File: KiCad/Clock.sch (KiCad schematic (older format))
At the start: 20 parts, among them SW2 SW_Push, SW3 SW_Push_SPDT, U44 NE555DR, U45 SN74LVC1G125DCK, U47 SN74LVC1G32DCK, U48 SN74LVC1G125DCK

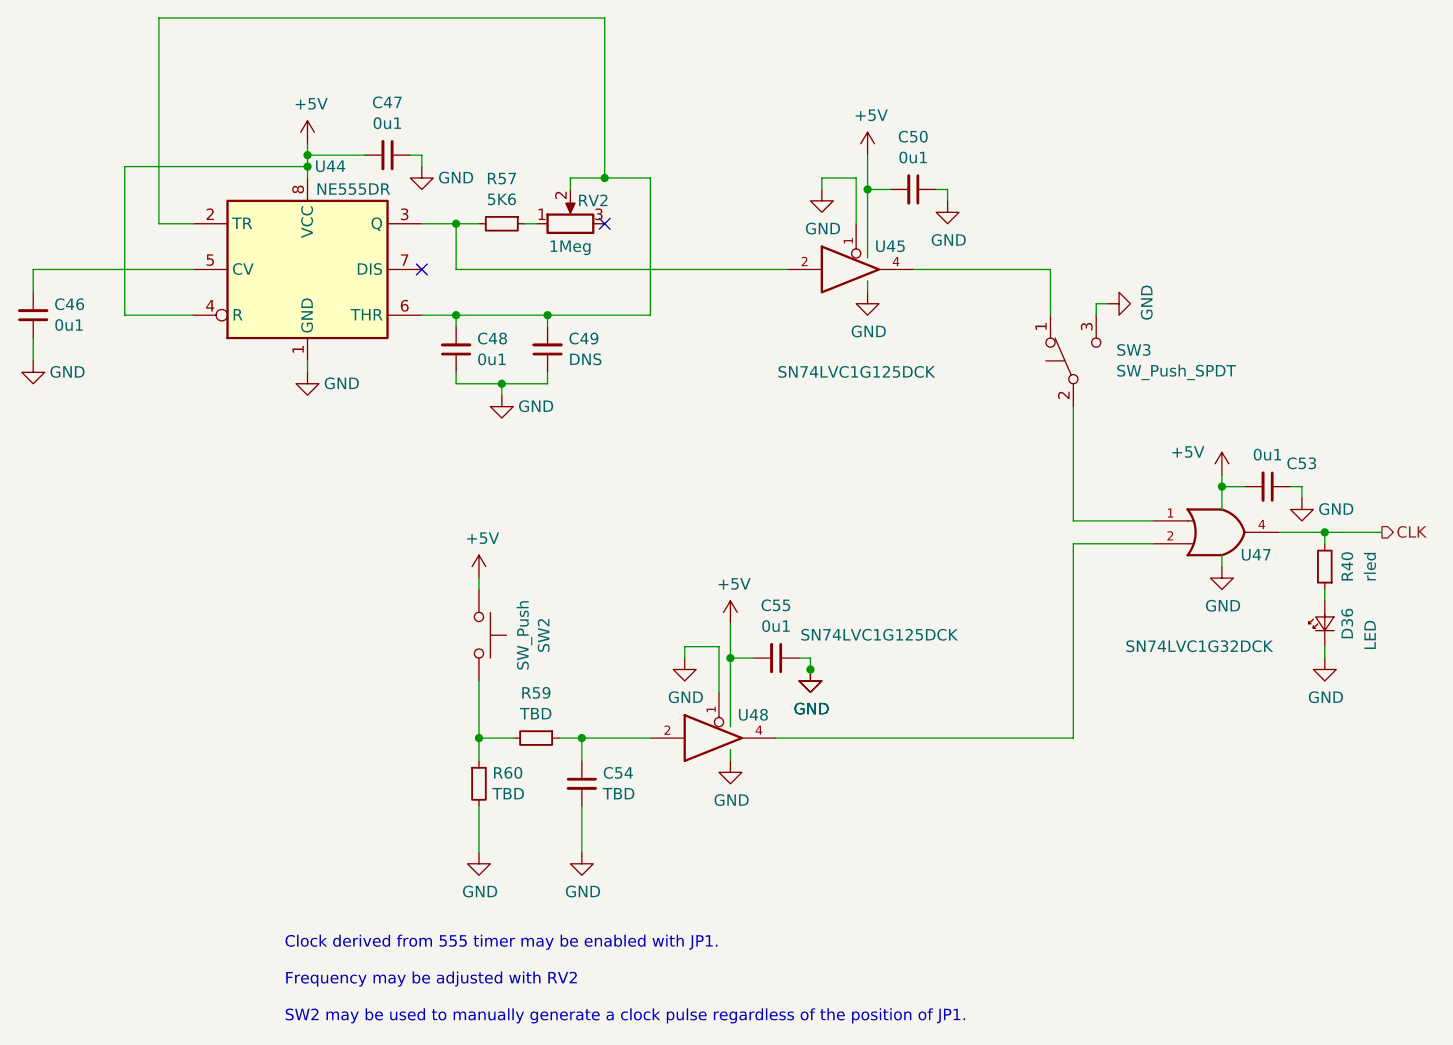
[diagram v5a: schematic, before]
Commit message: v0.3 Changed to Schmitt-Trigger ICs Added pull-down resistor to Clock Enable
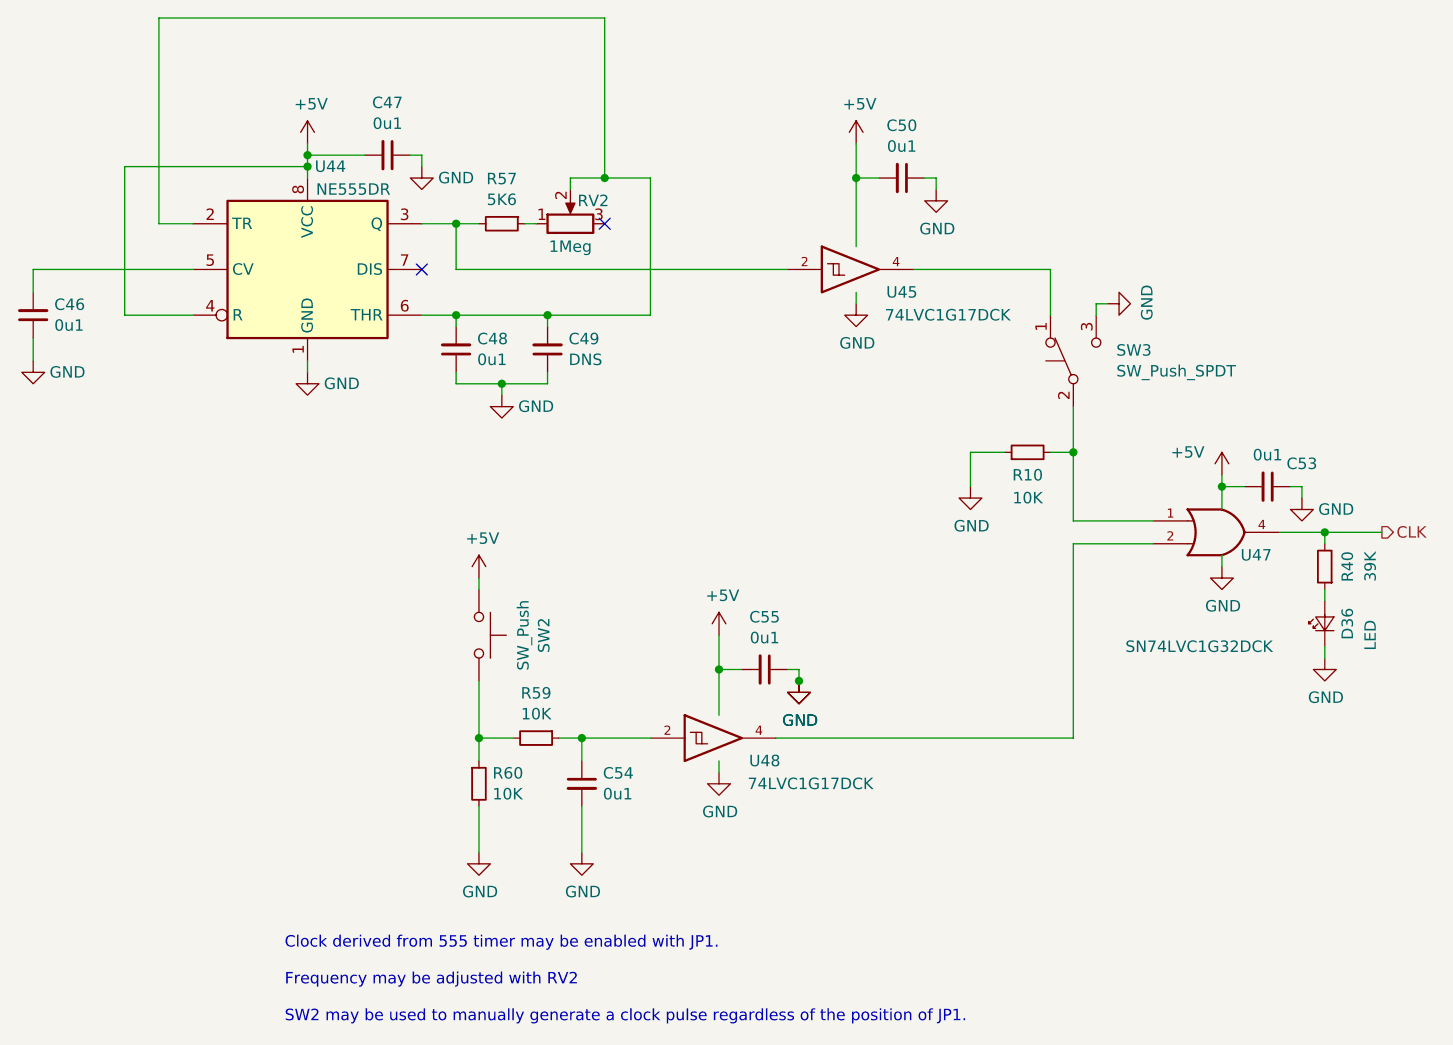
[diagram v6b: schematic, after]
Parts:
- removed U45, U48: SN74LVC1G125DCK, Package_TO_SOT_SMD:SOT-353_SC-70-5, symbol 74xGxx:74LVC1G125
- added R10: 10K, Resistor_SMD:R_0603_1608Metric, symbol Device:R_Small
- added U45, U48: 74LVC1G17DCK, Package_TO_SOT_SMD:SOT-353_SC-70-5, symbol 74xGxx:74LVC1G17
- C54: value TBD -> 0u1
- R40: value rled -> 39K
- R59, R60: value TBD -> 10K
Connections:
- net +5V: now also U45.5 (VCC), U48.5 (VCC)
- net GND: now also R10.1, U45.3 (GND), U48.3 (GND)
- net at SW3.2 (B), U47.1: now also R10.2
- net at U47.2: now also U48.4
- net at C54.1, R59.1: now also U48.2
- net at R57.2, U44.3 (Q): now also U45.2
- net at SW3.1 (A): now also U45.4
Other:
- moved on the sheet: C50, C55
